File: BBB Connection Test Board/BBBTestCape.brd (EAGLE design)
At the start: 59.7 x 46.7 mm, 29 parts, among them X0 SWTCH_BLCK, X1 SWTCH_BLCK

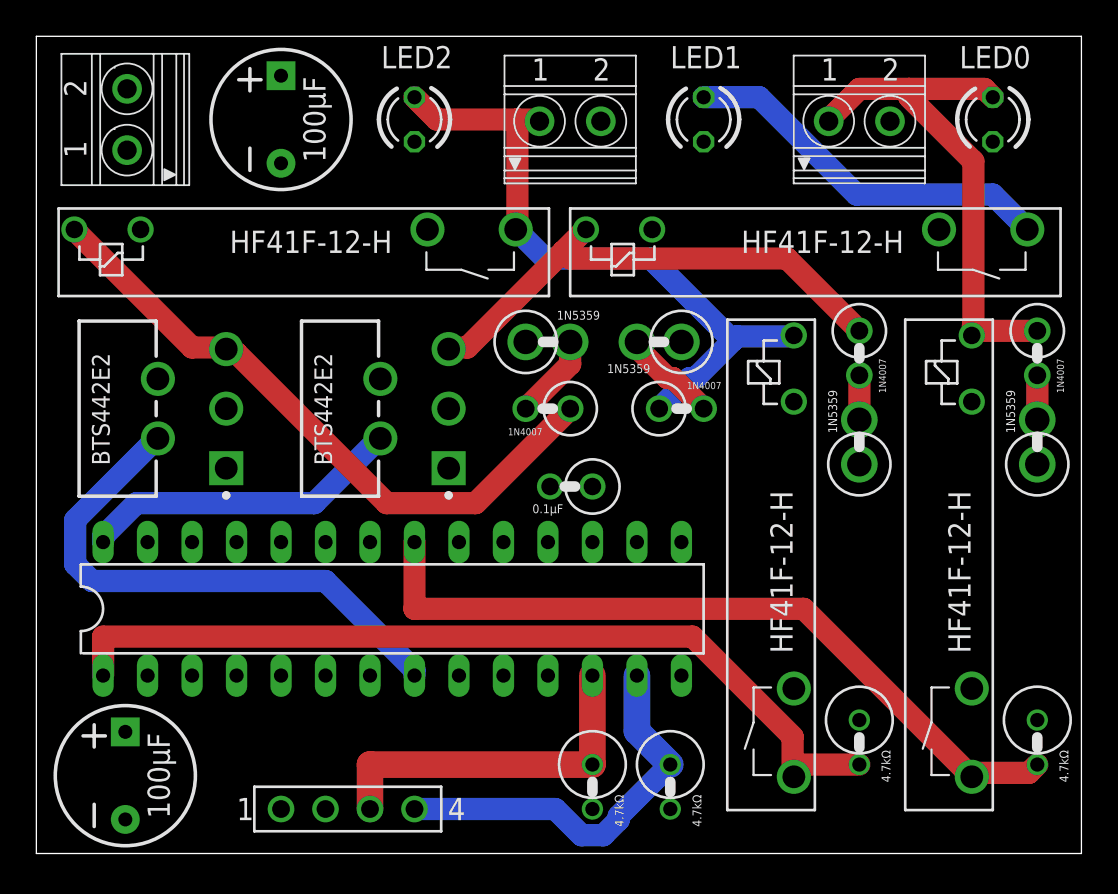
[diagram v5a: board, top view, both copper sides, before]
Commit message: Finalize BBB Connection Test Board Rev B. Sending this version to fab.
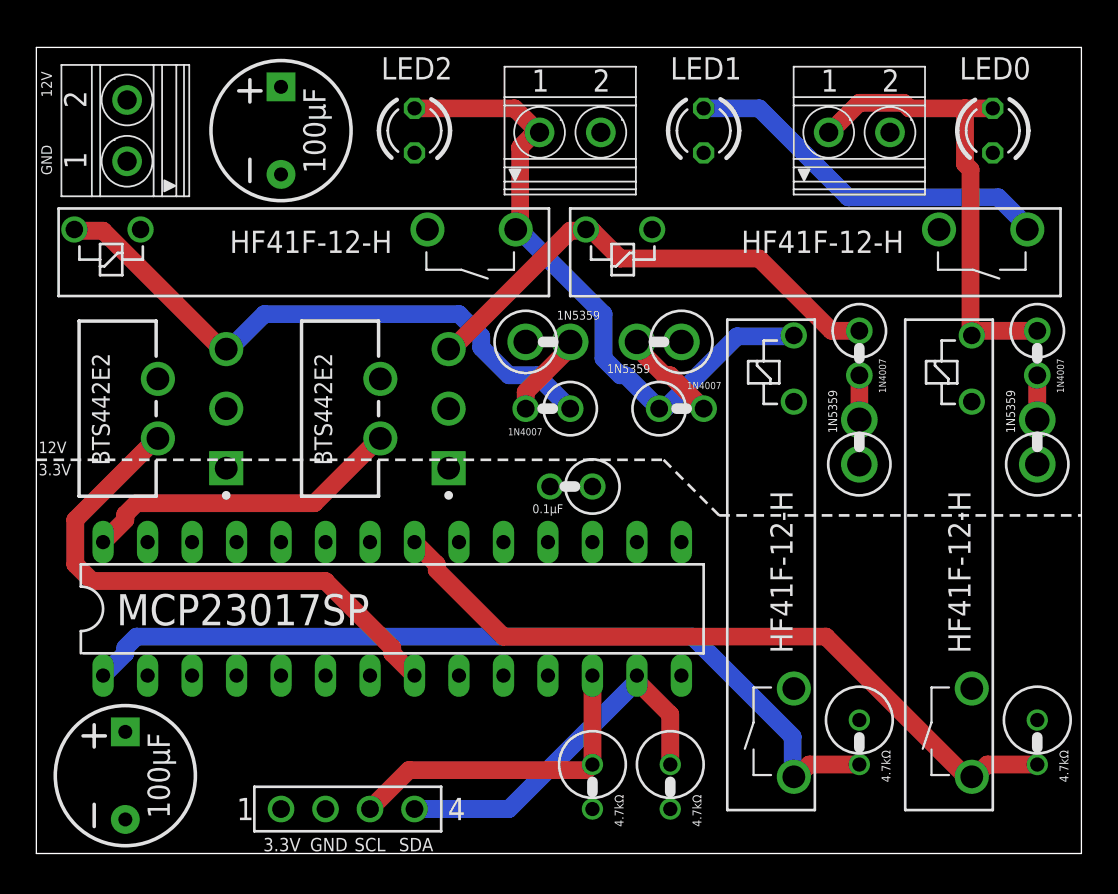
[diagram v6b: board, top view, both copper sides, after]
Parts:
- moved 12V_PWR_BLK:C1 0.63 mm to (14.0, 41.3)
- moved 12V_PWR_BLK:PWR 0.63 mm to (5.08, 41.3)
- moved LED0 0.63 mm to (54.6, 41.3)
- moved LED1 0.63 mm to (38.1, 41.3)
- moved LED2 0.63 mm to (21.6, 41.3)
- moved X0 0.63 mm to (47.0, 41.3)
- moved X1 0.63 mm to (30.5, 41.3)
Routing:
- net N$2: track 29.8 -> 27.1 mm
- net DUAL_12V⇆3V3_1BIT1:3V3_TO_12_1BIT1:N$1: track 37.0 -> 34.8 mm
- net N$7: track 43.6 -> 41.5 mm
- net BBB_IO1:SCL: track 20.3 -> 18.8 mm
- net N$5: track 50.4 -> 49.2 mm
- net N$3: track 38.5 -> 37.2 mm
- net BBB_IO1:SDA: track 22.9 -> 21.9 mm
- net 3V3_TO_12_1BIT1:N$1: track 29.4 -> 28.6 mm
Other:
- board size 59.7 x 46.7 mm -> 59.7 x 46 mm
